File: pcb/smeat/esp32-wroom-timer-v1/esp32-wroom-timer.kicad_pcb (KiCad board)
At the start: 2 copper layers, 74.4 x 51.2 mm, 62 parts, among them J1 Fan_connector, J2 Programming, J3 input power, J4 Conn_Coaxial, Q1 Q_NMOS_GSD, Q2 Q_NMOS_GSD, U1 ESP32-WROOM-32U, U10 RX5808, U11 RX5808, U12 MCP9804_MSOP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

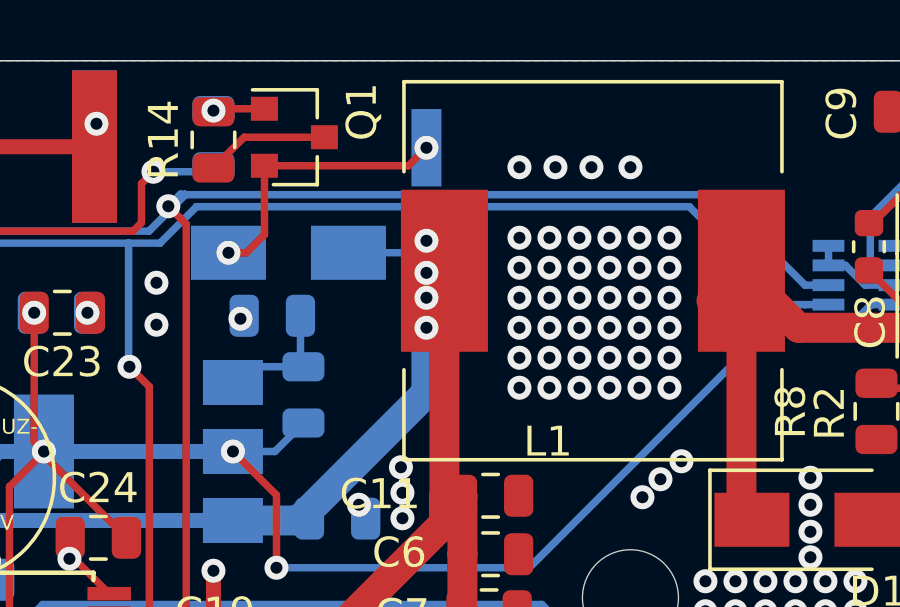
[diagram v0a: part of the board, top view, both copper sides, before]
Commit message: Add safety pullup resistors for i2c
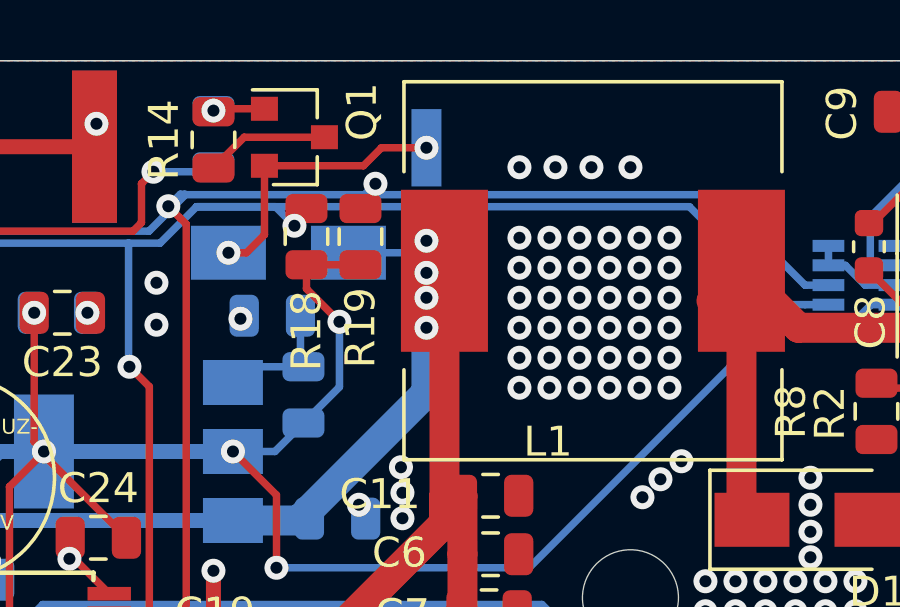
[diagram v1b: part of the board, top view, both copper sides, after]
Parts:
- added R18: 10k, Resistor_SMD:R_0805_2012Metric, F.Cu at (69.8, 58.7)
- added R19: 10k, Resistor_SMD:R_0805_2012Metric, F.Cu at (71.5, 58.7)
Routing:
- net +3V3: track 93.0 -> 101.0 mm, vias 7 -> 8
- net /SCL: track 57.9 -> 62.2 mm, vias 1 -> 2
- net /SDA: track 59.5 -> 61.0 mm, vias 1 -> 2
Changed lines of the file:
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@@
     (thickness 1.6)
     (drawings 18)
-    (tracks 947)
+    (tracks 965)
     (zones 0)
-    (modules 62)
+    (modules 64)
     (nets 92)
   )
@@
     (uvia_drill 0.1)
   )
+  (module Resistor_SMD:R_0805_2012Metric (layer F.Cu)
+    (at 71.55 58.6625 90)
+    (descr "Resistor SMD 0805 (2012 Metric), square (rectangular) end terminal, IPC_7351 nominal, (Body size source: https://docs.google.com/spreadsheets/d/1BsfQQcO9C6DZCsRaXUlFlo91Tg2WpOkGARC1WS5S8t0/edit?usp=sharing), generated with kicad-footprint-generator")
+    (tags resistor)
+    (attr smd)
+    (fp_text reference R19 (at -3.0375 0 90) (layer F.SilkS)
+      (effects (font (size 1 1) (thickness 0.15)))
+    )
+    (fp_text value 10k (at 0 1.65 90) (layer F.Fab)
+      (effects (font (size 1 1) (thickness 0.15)))
+    )
+    (fp_text user %R (at 0 0 90) (layer F.Fab)
+      (effects (font (size 0.5 0.5) (thickness 0.08)))
+    )
+    (fp_line (start 1.68 0.95) (end -1.68 0.95) (layer F.CrtYd) (width 0.05))
+    (fp_line (start 1.68 -0.95) (end 1.68 0.95) (layer F.CrtYd) (width 0.05))
+    (fp_line (start -1.68 -0.95) (end 1.68 -0.95) (layer F.CrtYd) (width 0.05))
+    (fp_line (start -1.68 0.95) (end -1.68 -0.95) (layer F.CrtYd) (width 0.05))
+    (fp_line (start -0.258578 0.71) (end 0.258578 0.71) (layer F.SilkS) (width 0.12))
+    (fp_line (start -0.258578 -0.71) (end 0.258578 -0.71) (layer F.SilkS) (width 0.12))
+    (fp_line (start 1 0.6) (end -1 0.6) (layer F.Fab) (width 0.1))
+    (fp_line (start 1 -0.6) (end 1 0.6) (layer F.Fab) (width 0.1))
+    (fp_line (start -1 -0.6) (end 1 -0.6) (layer F.Fab) (width 0.1))
+    (fp_line (start -1 0.6) (end -1 -0.6) (layer F.Fab) (width 0.1))
+    (pad 2 smd roundrect (at 0.9375 0 90) (size 0.975 1.4) (layers F.Cu F.Paste F.Mask) (roundrect_rratio 0.25)
+      (net 71 /SDA))
+    (pad 1 smd roundrect (at -0.9375 0 90) (size 0.975 1.4) (layers F.Cu F.Paste F.Mask) (roundrect_rratio 0.25)
+      (net 5 +3V3))
+    (model ${KISYS3DMOD}/Resistor_SMD.3dshapes/R_0805_2012Metric.wrl
+      (at (xyz 0 0 0))
+      (scale (xyz 1 1 1))
+      (rotate (xyz 0 0 0))
+    )
+  )
+  (module Resistor_SMD:R_0805_2012Metric (layer F.Cu)
+    (at 69.75 58.6625 90)
+    (descr "Resistor SMD 0805 (2012 Metric), square (rectangular) end terminal, IPC_7351 nominal, (Body size source: https://docs.google.com/spreadsheets/d/1BsfQQcO9C6DZCsRaXUlFlo91Tg2WpOkGARC1WS5S8t0/edit?usp=sharing), generated with kicad-footprint-generator")
+    (tags resistor)
+    (attr smd)
+    (fp_text reference R18 (at -3.1375 0 90) (layer F.SilkS)
+      (effects (font (size 1 1) (thickness 0.15)))
+    )
+    (fp_text value 10k (at 0 1.65 90) (layer F.Fab)
+      (effects (font (size 1 1) (thickness 0.15)))
+    )
+    (fp_text user %R (at 0 0 90) (layer F.Fab)
+      (effects (font (size 0.5 0.5) (thickness 0.08)))
+    )
+    (fp_line (start 1.68 0.95) (end -1.68 0.95) (layer F.CrtYd) (width 0.05))
+    (fp_line (start 1.68 -0.95) (end 1.68 0.95) (layer F.CrtYd) (width 0.05))
+    (fp_line (start -1.68 -0.95) (end 1.68 -0.95) (layer F.CrtYd) (width 0.05))
+    (fp_line (start -1.68 0.95) (end -1.68 -0.95) (layer F.CrtYd) (width 0.05))
+    (fp_line (start -0.258578 0.71) (end 0.258578 0.71) (layer F.SilkS) (width 0.12))
+    (fp_line (start -0.258578 -0.71) (end 0.258578 -0.71) (layer F.SilkS) (width 0.12))
+    (fp_line (start 1 0.6) (end -1 0.6) (layer F.Fab) (width 0.1))
+    (fp_line (start 1 -0.6) (end 1 0.6) (layer F.Fab) (width 0.1))
+    (fp_line (start -1 -0.6) (end 1 -0.6) (layer F.Fab) (width 0.1))
+    (fp_line (start -1 0.6) (end -1 -0.6) (layer F.Fab) (width 0.1))
+    (pad 2 smd roundrect (at 0.9375 0 90) (size 0.975 1.4) (layers F.Cu F.Paste F.Mask) (roundrect_rratio 0.25)
+      (net 70 /SCL))
+    (pad 1 smd roundrect (at -0.9375 0 90) (size 0.975 1.4) (layers F.Cu F.Paste F.Mask) (roundrect_rratio 0.25)
+      (net 5 +3V3))
+    (model ${KISYS3DMOD}/Resistor_SMD.3dshapes/R_0805_2012Metric.wrl
+      (at (xyz 0 0 0))
+      (scale (xyz 1 1 1))
+      (rotate (xyz 0 0 0))
+    )
+  )
   (module Diode_SMD:D_SMA (layer B.Cu)
     (at 69.15 59.2 180)
@@
   (segment (start 61 65.85) (end 61 65.825) (width 0.25) (layer F.Cu) (net 5))
   (segment (start 59.85 67) (end 61 65.85) (width 0.25) (layer F.Cu) (net 5))
+  (segment (start 69.75 59.6) (end 71.55 59.6) (width 0.25) (layer F.Cu) (net 5))
+  (via (at 70.85 61.5) (size 0.8) (drill 0.4) (layers F.Cu B.Cu) (net 5))
+  (segment (start 69.75 59.6) (end 69.75 60.4) (width 0.25) (layer F.Cu) (net 5))
+  (segment (start 69.75 60.4) (end 70.85 61.5) (width 0.25) (layer F.Cu) (net 5))
+  (segment (start 70.85 63.675) (end 69.65 64.875) (width 0.25) (layer B.Cu) (net 5))
+  (segment (start 70.85 61.5) (end 70.85 63.675) (width 0.25) (layer B.Cu) (net 5))
   (via (at 40.61 54) (size 0.8) (drill 0.4) (layers F.Cu B.Cu) (net 6))
   (segment (start 40.61 54) (end 40.61 54.55) (width 0.25) (layer F.Cu) (net 6))
@@
   (segment (start 33.52 65.015) (end 34.12 65.015) (width 0.25) (layer F.Cu) (net 39))
   (via (at 73.75 55.7) (size 0.8) (drill 0.4) (layers F.Cu B.Cu) (net 46))
-  (segment (start 68.35 56.3) (end 73.15 56.3) (width 0.25) (layer F.Cu) (net 46))
-  (segment (start 73.15 56.3) (end 73.75 55.7) (width 0.25) (layer F.Cu) (net 46))
   (segment (start 68.35 56.3) (end 68.35 58.6) (width 0.25) (layer F.Cu) (net 46))
   (segment (start 68.35 58.6) (end 67.75 59.2) (width 0.25) (layer F.Cu) (net 46))
   (via (at 67.15 59.2) (size 0.8) (drill 0.4) (layers F.Cu B.Cu) (net 46))
   (segment (start 67.75 59.2) (end 67.15 59.2) (width 0.25) (layer F.Cu) (net 46))
+  (segment (start 73 55.7) (end 73.75 55.7) (width 0.25) (layer F.Cu) (net 46))
+  (segment (start 72.250998 55.7) (end 73 55.7) (width 0.25) (layer F.Cu) (net 46))
+  (segment (start 71.650998 56.3) (end 72.250998 55.7) (width 0.25) (layer F.Cu) (net 46))
+  (segment (start 68.35 56.3) (end 71.650998 56.3) (width 0.25) (layer F.Cu) (net 46))
   (segment (start 66.65 54.4625) (end 66.65 54.4625) (width 0.25) (layer B.Cu) (net 47))
   (via (at 66.65 54.4625) (size 0.8) (drill 0.4) (layers F.Cu B.Cu) (net 47))
@@
   (segment (start 64.869989 58.880011) (end 66.084988 57.665012) (width 0.25) (layer B.Cu) (net 70))
   (segment (start 63.82069 58.880011) (end 64.869989 58.880011) (width 0.25) (layer B.Cu) (net 70))
+  (via (at 69.349998 58.3) (size 0.8) (drill 0.4) (layers F.Cu B.Cu) (net 70))
+  (segment (start 66.084988 57.665012) (end 68.71501 57.665012) (width 0.25) (layer B.Cu) (net 70))
+  (segment (start 68.71501 57.665012) (end 69.349998 58.3) (width 0.25) (layer B.Cu) (net 70))
+  (segment (start 69.349998 58.125002) (end 69.75 57.725) (width 0.25) (layer F.Cu) (net 70))
+  (segment (start 69.349998 58.3) (end 69.349998 58.125002) (width 0.25) (layer F.Cu) (net 70))
   (segment (start 86.37 60.28) (end 83.355001 57.265001) (width 0.25) (layer B.Cu) (net 71))
   (segment (start 87.15 60.28) (end 86.37 60.28) (width 0.25) (layer B.Cu) (net 71))
-  (segment (start 83.355001 57.265001) (end 65.715001 57.265001) (width 0.25) (layer B.Cu) (net 71))
   (segment (start 65.715001 57.265001) (end 64.500002 58.48) (width 0.25) (layer B.Cu) (net 71))
   (segment (start 52.749313 58.48) (end 49.5 55.230687) (width 0.25) (layer B.Cu) (net 71))
@@
   (segment (start 63.175 72.515) (end 64.15 72.515) (width 0.25) (layer F.Cu) (net 71))
   (via (at 65.145612 57.649779) (size 0.8) (drill 0.4) (layers F.Cu B.Cu) (net 71))
+  (via (at 72.05 56.9) (size 0.8) (drill 0.4) (layers F.Cu B.Cu) (net 71))
+  (segment (start 71.684999 57.265001) (end 72.05 56.9) (width 0.25) (layer B.Cu) (net 71))
+  (segment (start 71.684999 57.265001) (end 65.715001 57.265001) (width 0.25) (layer B.Cu) (net 71))
+  (segment (start 83.355001 57.265001) (end 71.684999 57.265001) (width 0.25) (layer B.Cu) (net 71))
+  (segment (start 72.05 57.225) (end 71.55 57.725) (width 0.25) (layer F.Cu) (net 71))
+  (segment (start 72.05 56.9) (end 72.05 57.225) (width 0.25) (layer F.Cu) (net 71))
   (segment (start 60.295276 71.589023) (end 60.959332 70.924968) (width 0.25) (layer B.Cu) (net 72))
   (segment (start 46.96 71.1) (end 46.96 71.775002) (width 0.25) (layer B.Cu) (net 72))

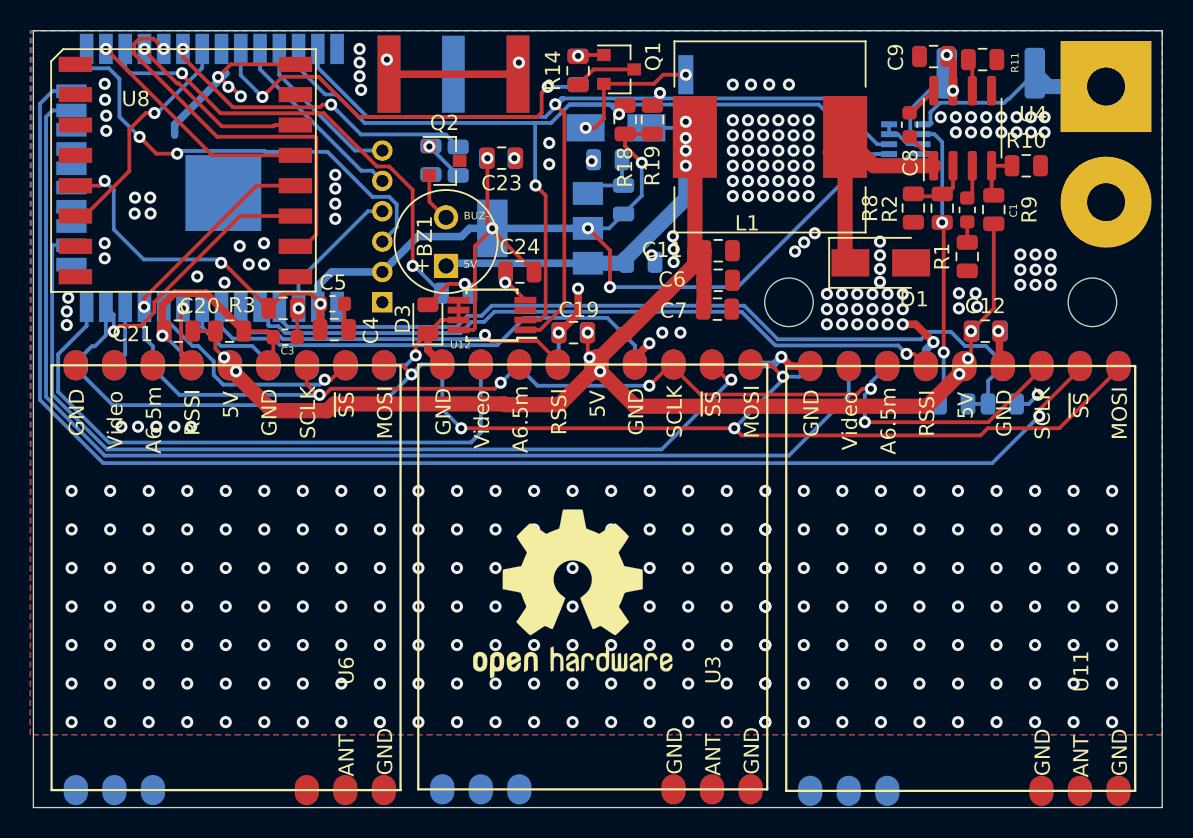
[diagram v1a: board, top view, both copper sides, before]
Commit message: Last minute PCB changes I hate those :/
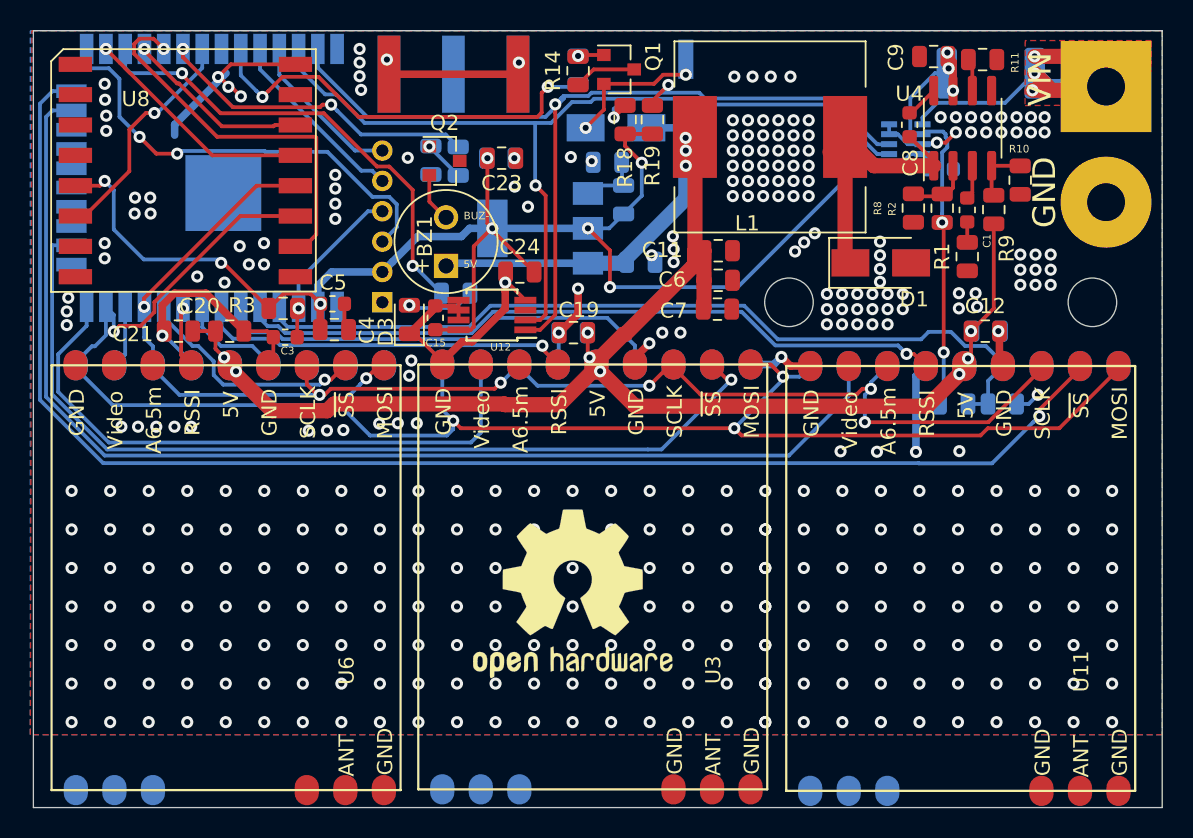
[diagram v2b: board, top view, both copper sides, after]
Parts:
- added C14: 0.1µF, Capacitor_SMD:C_0603_1608Metric, B.Cu at (90.6, 61.9)
- added C15: 0.1µF, Capacitor_SMD:C_0603_1608Metric, F.Cu at (57.2, 71.7)
- R18, R19: value 10k -> 4K7
- moved D3 1.22 mm to (55.5, 71.8)
- moved R10 1.03 mm to (95.8, 62.6), turned to 270 degrees
- moved J1 1.02 mm to (73.8, 56.8)
- moved R13 0.18 mm to (68.6, 61.5)
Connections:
- U1 pad 6: /ADC3 -> /ADC4
- U1 pad 7: /ADC4 -> /ADC3
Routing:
- net +BATT: track 14.4 -> 25.8 mm, vias 0 -> 3
- net GND: track 71.6 -> 81.4 mm, vias 350 -> 362
- net /MOSI: track 110.2 -> 113.3 mm
- net +3V3: track 101.0 -> 103.7 mm
- net +5V: track 118.4 -> 120.3 mm, vias 12 -> 11
- net /ADC4: track 31.7 -> 30.2 mm
- net /SCL: track 62.2 -> 60.7 mm
- net Net-(D3-Pad2): track 2.99 -> 4.47 mm
- net +28V: track 27.1 -> 28.5 mm, vias 4 -> 5
- net /ADC3: track 23.6 -> 24.6 mm
- net /SDA: track 61.0 -> 61.9 mm
- added copper zone on F.Cu, net +BATT
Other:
- board text added: "VIN"
